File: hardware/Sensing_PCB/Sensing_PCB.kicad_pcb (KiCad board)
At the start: 2 copper layers, 3 parts, among them U1 FSG005WNPB, U3 LMC6484IN_NOPB, U4 Pico

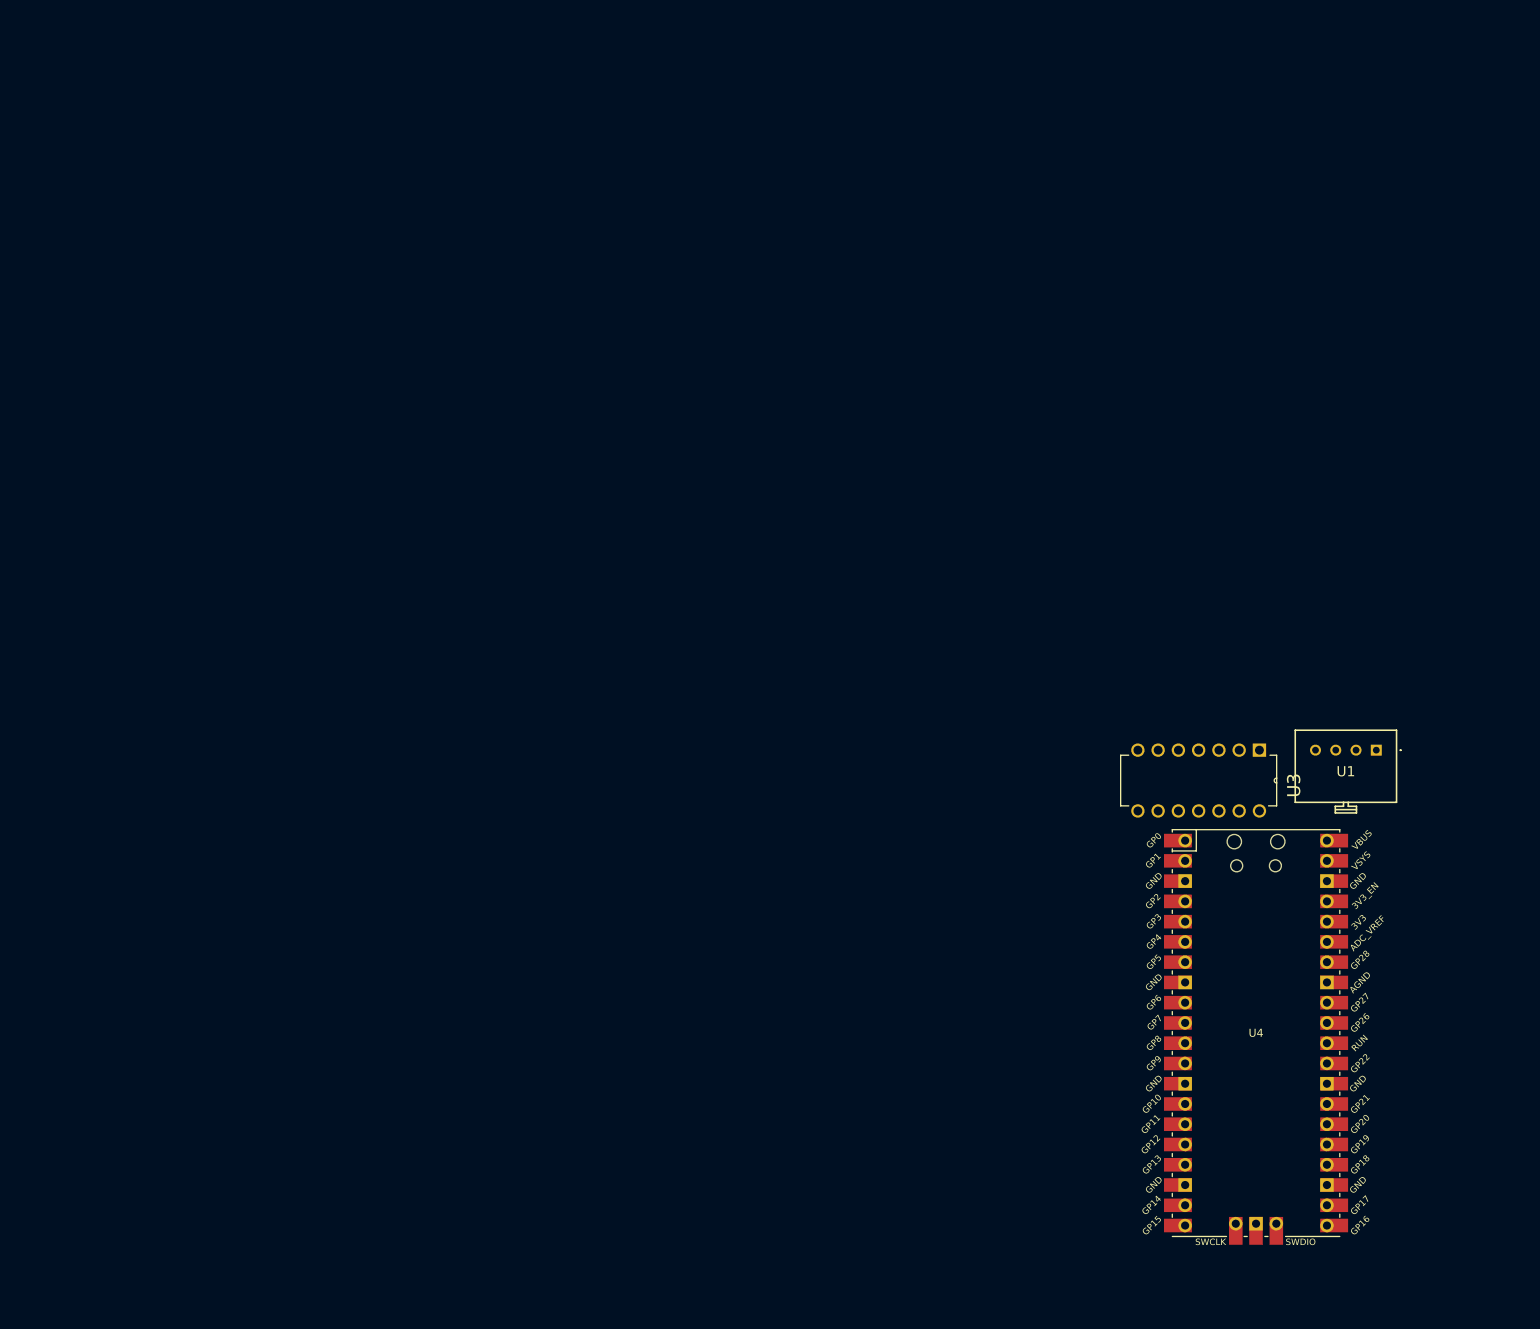
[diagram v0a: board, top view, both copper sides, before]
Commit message: Add KiCad project for receiver PCB
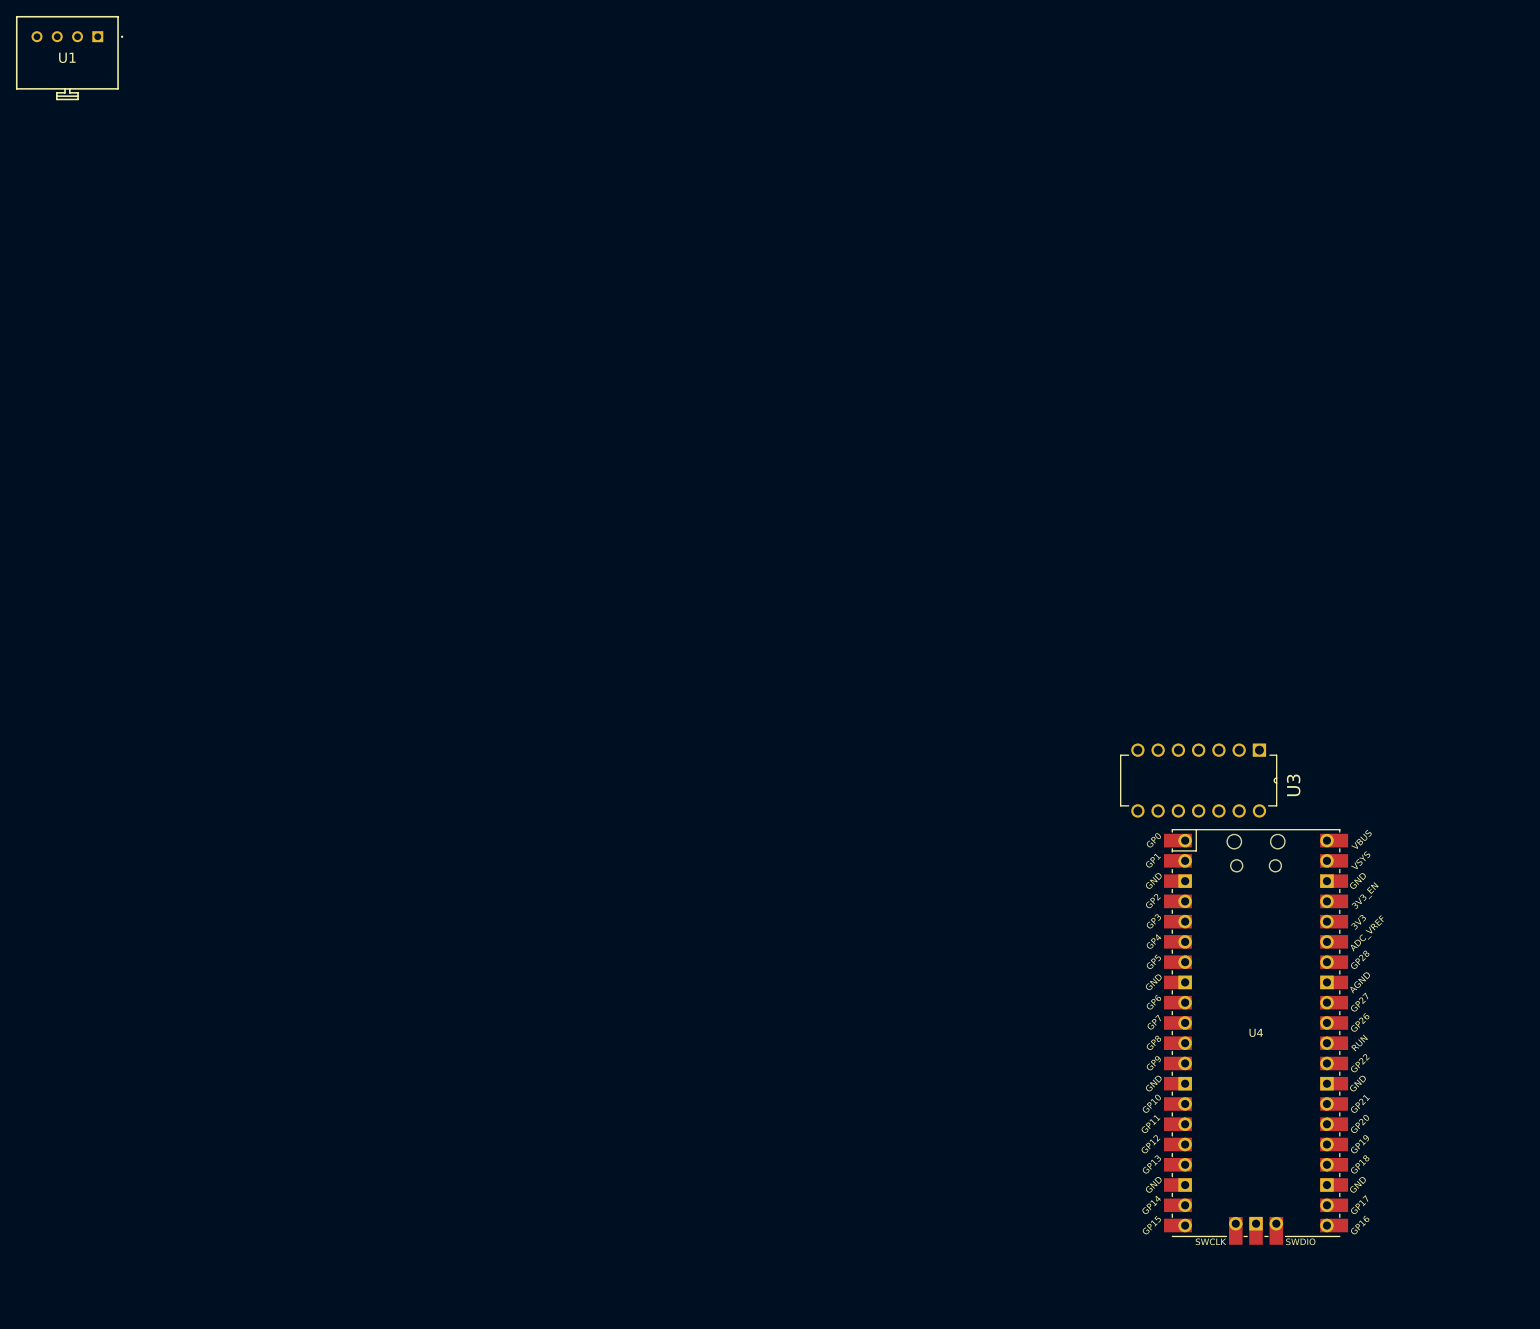
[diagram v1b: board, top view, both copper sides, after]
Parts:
- moved U1 183.6 mm to (11.2, 3.55)
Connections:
- U1 pad 1: /3V3_Chamber -> unconnected-(U1-SUPPLY_VS_(+)-Pad1)
- U1 pad 2: /FS_OUTPUT(+) -> unconnected-(U1-OUTPUT_VO_(+)-Pad2)
- U1 pad 3: GND -> unconnected-(U1-GROUND_VG_(-)-Pad3)
- U1 pad 4: /FS_OUPUT(-) -> unconnected-(U1-OUTPUT_VO_(-)-Pad4)

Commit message: Add Rev.1 of Sender PCB
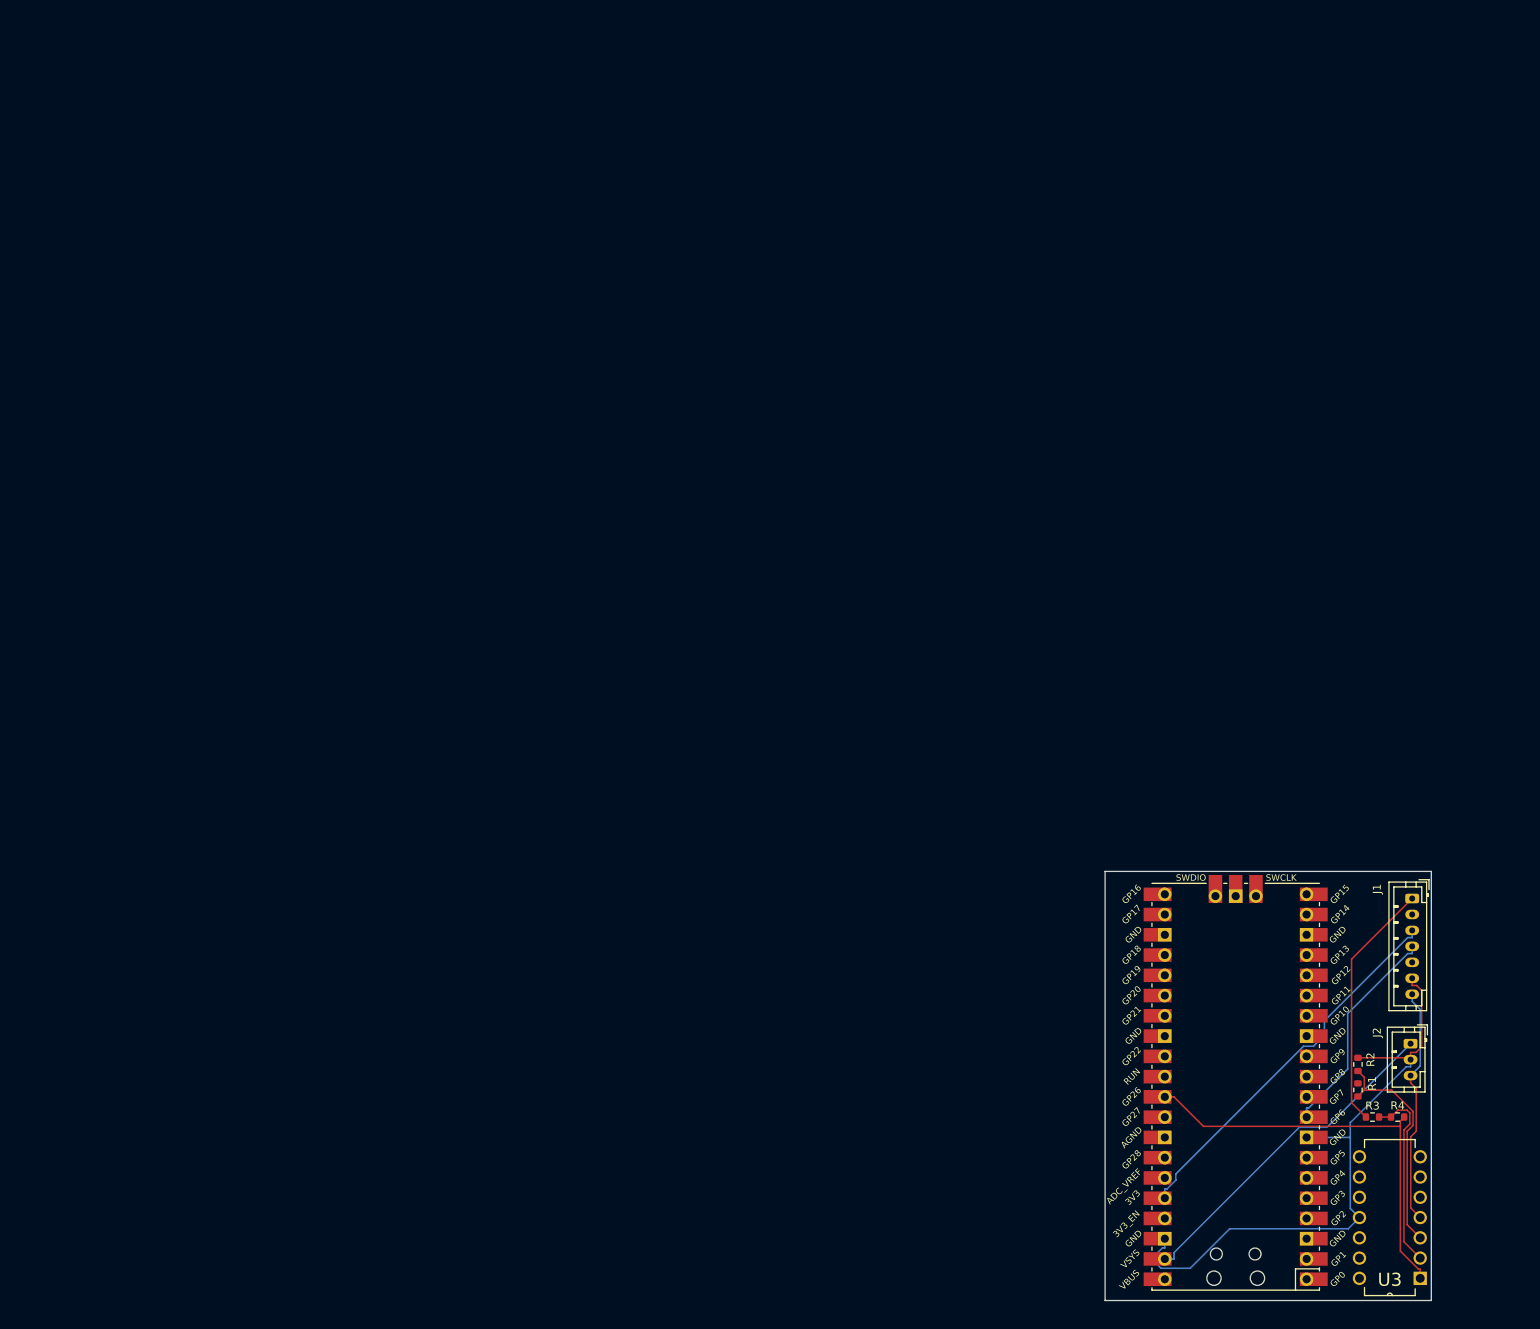
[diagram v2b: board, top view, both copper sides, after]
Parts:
- removed U1: FSG005WNPB, FSG005WNPB:FSG005WNPB
- added G***: LOGO, assets:opel_logo, B.Cu at (154.0, 122.4)
- added J1: Conn_01x07_Socket, Connector_JST:JST_PH_B7B-PH-K_1x07_P2.00mm_Vertical, F.Cu at (176.0, 111.6)
- added J2: Conn_01x03_Socket, Connector_JST:JST_PH_B3B-PH-K_1x03_P2.00mm_Vertical, F.Cu at (175.8, 129.8)
- added R1: 10k, Resistor_SMD:R_0603_1608Metric, F.Cu at (169.2, 135.6)
- added R2: 50k, Resistor_SMD:R_0603_1608Metric, F.Cu at (169.2, 132.4)
- added R3: 10k, Resistor_SMD:R_0603_1608Metric, F.Cu at (171.0, 139.0)
- added R4: 50k, Resistor_SMD:R_0603_1608Metric, F.Cu at (174.2, 139.0)
- moved U3 51.5 mm to (169.4, 144.0), turned to 180 degrees
- moved U4 7.20 mm to (153.9, 135.2), turned to 180 degrees
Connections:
- U3 pad 11: GND -> /GND
- U3 pad 2: Net-(U3-NEG1) -> /OUT1
- U4 pad 38: GND -> /GND
- U4 pad 4: unconnected-(U4-GPIO2-Pad4) -> /I2C1_SDA
- U4 pad 5: unconnected-(U4-GPIO3-Pad5) -> /I2C1_SCL
- U4 pad 6: unconnected-(U4-GPIO4-Pad6) -> /I2C0_SDA
- U4 pad 7: unconnected-(U4-GPIO5-Pad7) -> /I2C0_SCL
- U4 pad 8: unconnected-(U4-GND-Pad8) -> /GND
- U4 pad 9: unconnected-(U4-GPIO6-Pad9) -> /SERVO
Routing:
- net /GND: track 0.00 -> 80.0 mm
- net /ADC: track 0.00 -> 52.6 mm
- net /3V3_Chamber: track 0.00 -> 47.6 mm
- net /3V3: track 0.00 -> 42.5 mm
- net /FS_OUPUT(-): track 0.00 -> 31.3 mm
- net /5V: track 0.00 -> 30.0 mm
- net Net-(U3-POS1): track 0.00 -> 27.9 mm
- net /SERVO: track 0.00 -> 27.4 mm
- net /OUT1: track 0.00 -> 23.7 mm
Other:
- board outline added: 40.9 x 53.8 mm
- board text added: "Designed By Jun Park"
- board text added: "Low-Cost Thrust Stand Sensing Sender"
- board text added: "Rev 1.0"

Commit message: Update Sender PCB
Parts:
- added H1: MountingHole, MountingHole:MountingHole_2.2mm_M2, F.Cu at (136.5, 112.0)
- added H2: MountingHole, MountingHole:MountingHole_2.2mm_M2, F.Cu at (136.5, 157.5)
- added H3: MountingHole, MountingHole:MountingHole_2.2mm_M2, F.Cu at (187.0, 112.0)
- added H4: MountingHole, MountingHole:MountingHole_2.2mm_M2, F.Cu at (187.0, 157.5)
- added J3: Conn_01x03_Socket, Connector_JST:JST_PH_B3B-PH-K_1x03_P2.00mm_Vertical, F.Cu at (136.0, 146.5)
- G1: renamed from G***; moved to F.Cu
- J2: value Conn_01x03_Socket -> Conn_01x04_Socket; footprint Connector_JST:JST_PH_B3B-PH-K_1x03_P2.00mm_Vertical -> Connector_JST:JST_PH_B4B-PH-K_1x04_P2.00mm_Vertical
- moved J1 47.7 mm to (136.0, 137.5), turned to 90 degrees
- moved G1 23.4 mm to (176.5, 116.0), turned to 0 degrees
- moved R2 15.1 mm to (183.0, 138.5)
- moved R3 14.7 mm to (183.0, 130.5), turned to 90 degrees
- moved J2 14.6 mm to (187.0, 120.5)
- moved R1 13.9 mm to (183.0, 134.0)
- moved U3 10.3 mm to (178.3, 149.1), turned to 0 degrees
- moved R4 6.20 mm to (168.5, 136.5), turned to 90 degrees
- turned U4 to 0 degrees
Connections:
- J1 pad 1: /FS_OUPUT(-) -> /GND
- J1 pad 2: /FS_OUPUT(+) -> /I2C1_SDA
- J1 pad 3: /3V3_Chamber -> /I2C1_SCL
- J1 pad 4: /SERVO -> /I2C0_SDA
- J1 pad 5: unconnected-(J1-Pin_5-Pad5) -> /I2C0_SCL
- J1 pad 6: /GND -> /3V3
- J2 pad 1: /3V3 -> /3V3_Chamber
- J2 pad 2: /GND -> /FS_OUTPUT(+)
- J2 pad 3: /5V -> /GND
- R3 pad 2: /FS_OUPUT(-) -> /FS_OUTPUT(-)
- U3 pad 4: /5V -> /3V3_Chamber
- U4 pad 23: unconnected-(U4-GND-Pad23)_1 -> /GND
- U4 pad 28: unconnected-(U4-GND-Pad28)_1 -> /GND
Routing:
- net /3V3_Chamber: track 47.6 -> 0.00 mm
- net /ADC: track 52.6 -> 9.99 mm
- net /GND: track 80.0 -> 46.6 mm
- net /FS_OUPUT(-): track 31.3 -> 0.00 mm
- net /I2C1_SDA: track 0.00 -> 22.7 mm
- net /FS_OUTPUT(+): track 0.00 -> 18.7 mm
- net /I2C1_SCL: track 0.00 -> 18.2 mm
- net /I2C0_SCL: track 0.00 -> 13.7 mm
- net /I2C0_SDA: track 0.00 -> 12.8 mm
- net /SERVO: track 27.4 -> 15.0 mm
- net /3V3: track 42.5 -> 32.5 mm
- net Net-(U3-POS1): track 27.9 -> 18.3 mm
- net /5V: track 30.0 -> 21.0 mm
- net /FS_OUTPUT(-): track 0.00 -> 5.42 mm
- net /OUT1: track 23.7 -> 21.6 mm
- added copper zone on B.Cu, net /3V3_Chamber
- added copper zone on F.Cu, net /GND
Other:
- board size 40.9 x 53.8 mm -> 56.5 x 56 mm

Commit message: New Sender Design
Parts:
- G1: moved to B.Cu
- R1, R2, R3, R4: footprint Resistor_SMD:R_0603_1608Metric -> Resistor_THT:R_Axial_DIN0207_L6.3mm_D2.5mm_P10.16mm_Horizontal
- moved G1 29.7 mm to (153.9, 135.2), turned to 180 degrees
- moved R1 20.1 mm to (176.5, 115.0)
- moved J2 16.8 mm to (173.5, 110.5), turned to 0 degrees
- moved R2 15.1 mm to (183.0, 153.6), turned to 90 degrees
- moved R4 15.1 mm to (183.0, 140.6)
- moved R3 5.31 mm to (183.0, 125.2)
- moved U3 1.50 mm to (178.3, 150.6)
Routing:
- net /GND: track 46.6 -> 0.00 mm
- net /ADC: track 9.99 -> 23.5 mm
- net /FS_OUTPUT(+): track 18.7 -> 5.44 mm
- net Net-(U3-POS1): track 18.3 -> 29.5 mm
- net /OUT1: track 21.6 -> 28.9 mm
- net /I2C0_SDA: track 12.8 -> 17.1 mm
- net /I2C0_SCL: track 13.7 -> 10.8 mm
- net /I2C1_SCL: track 18.2 -> 16.4 mm
- net /FS_OUTPUT(-): track 5.42 -> 6.50 mm
- net /3V3: track 32.5 -> 33.0 mm
